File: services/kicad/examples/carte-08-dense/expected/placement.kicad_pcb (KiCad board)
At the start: 2 copper layers, 125 x 95 mm, 56 parts, among them J1 IN_5V, J10 IO0, J11 IO1, J12 IO2, J13 IO3, J14 IO4, J2 SWD, U1 STM32F103C8T6, U2 AMS1117-3.3

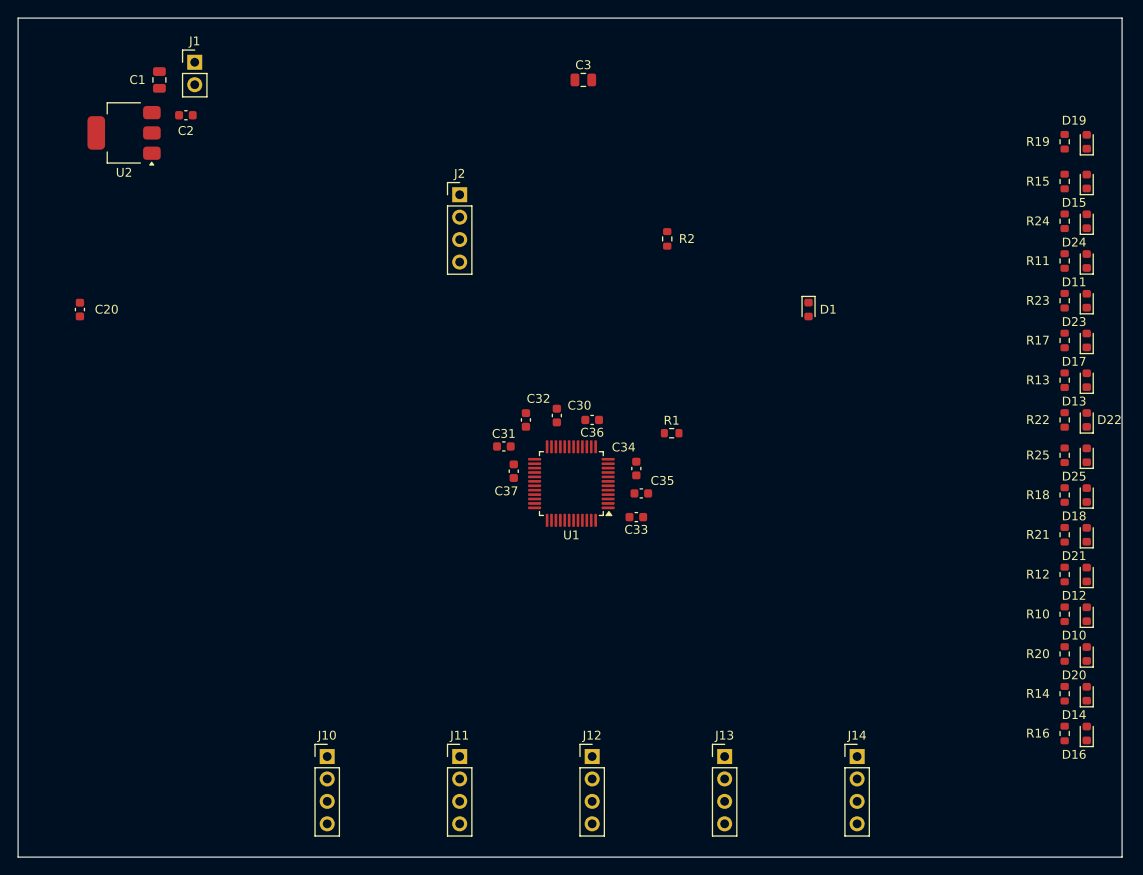
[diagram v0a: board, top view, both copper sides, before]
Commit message: feat(placement): les peripheriques se REPARTISSENT, ils ne s empilent plus
Question de l utilisateur devant le rendu : « c est quoi ce type de placement ? ».
Les composants s entassaient d un seul cote du boitier, etiquettes de
serigraphie l une sur l autre, trois quarts de la couronne vides.

TROIS CAUSES, toutes dans `_poser_les_peripheriques`, toutes la meme faute —
un angle unique pour tout un groupe :

  - les DIRECTS qui visent la meme broche (tous les decouplages d un rail,
    toutes les resistances d un meme signal) recevaient le MEME `angle_vers`
    et le meme rayon de depart ;
  - les SUIVEURS d un meme parent recevaient tous atan2(parent - centre) ;
  - les ISOLES partaient tous de l angle 0.0, c est-a-dire du meme point.

`le_long_du_rayon` ne s ecartait qu une fois la place prise : d ou la file.

REMEDE : `_ecart_en_eventail`. Le PREMIER de chaque groupe garde EXACTEMENT la
direction calculee — c est la topologie, on ne la perd pas pour faire joli — et
les suivants s ecartent symetriquement de 3 x `_PAS_ANGLE_DEG`.
Rien de deja pose ne bouge : seul l ANGLE DE DEPART de la recherche change, et
`le_long_du_rayon` reste seul juge de ce qui est libre.

BANC DES DIX CARTES, contour resserre ET peripheriques repartis :

    carte             demandee    livree         err  manq
    carte-01           25 x 20    20,1 x 13,6     0    0
    carte-02           55 x 40    34,9 x 25,2     0    0
    carte-03           50 x 35    27,6 x 19,9     0    0
    carte-04           60 x 45    36,6 x 29,8     0    0
    carte-05           70 x 50    40,0 x 32,6     0    0
    carte-06           80 x 60    46,5 x 36,4     0    0
    carte-07          110 x 80    47,7 x 38,8     0    0
    carte-08          125 x 95    57,4 x 44,1     0    0
    carte-09          130 x 100   57,8 x 45,2     0    0
    carte-10          140 x 105   59,0 x 45,8     0    0

Dix sur dix, 100 % route. carte-07 gagne 5,5 mm de largeur sur le passage
precedent, carte-06 deux, carte-10 deux. Sur ca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
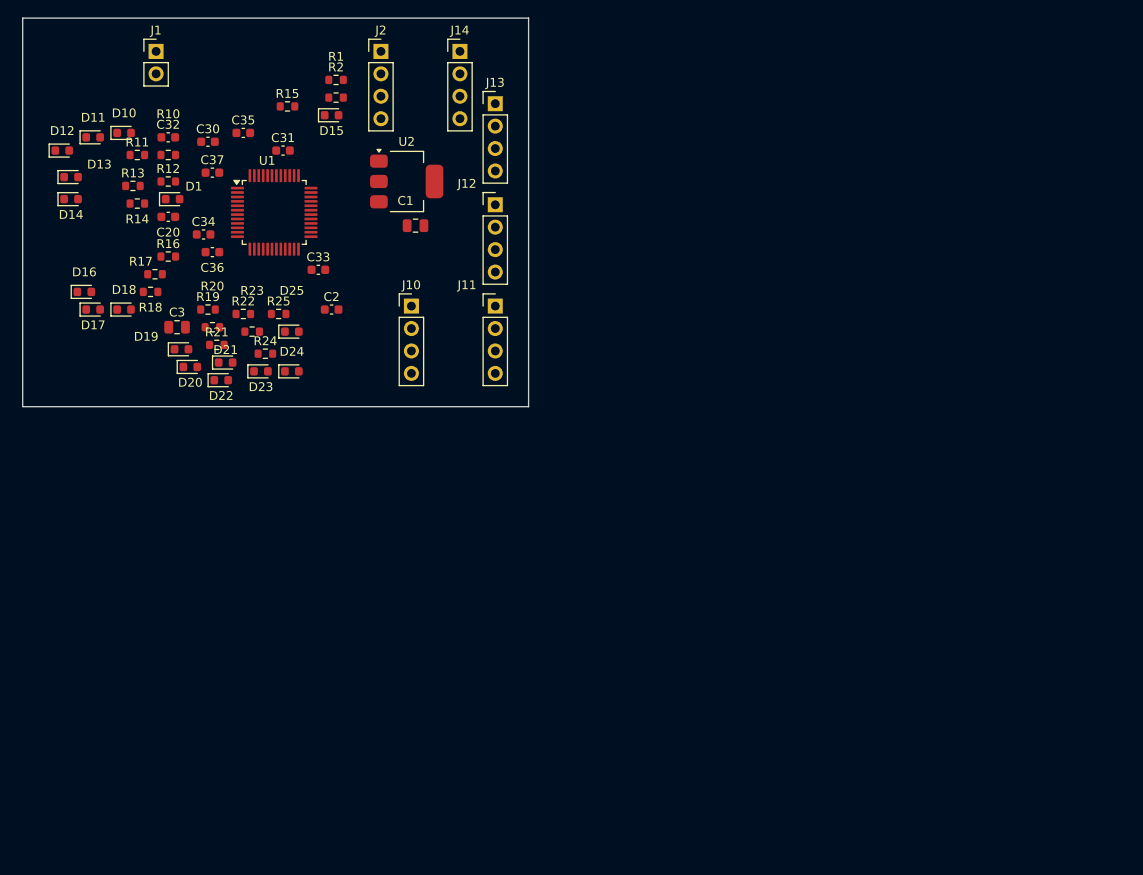
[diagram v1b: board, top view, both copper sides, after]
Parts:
- moved D14 127.9 mm to (92.0, 78.0), turned to 0 degrees
- moved D12 125.5 mm to (91.0, 72.5), turned to 0 degrees
- moved D16 124.0 mm to (93.5, 88.5), turned to 0 degrees
- moved D10 121.9 mm to (98.0, 70.5), turned to 0 degrees
- moved R14 118.8 mm to (99.5, 78.5), turned to 0 degrees
- moved D13 117.3 mm to (92.0, 75.5), turned to 0 degrees
- moved R16 115.0 mm to (103.0, 84.5), turned to 0 degrees
- moved R10 114.0 mm to (103.0, 73.0), turned to 0 degrees
- moved D11 113.4 mm to (94.5, 71.0), turned to 0 degrees
- moved D17 112.6 mm to (94.5, 90.5), turned to 0 degrees
- moved D18 111.0 mm to (98.0, 90.5), turned to 0 degrees
- moved R12 110.8 mm to (103.0, 76.0), turned to 0 degrees
- moved R13 107.8 mm to (99.0, 76.5), turned to 0 degrees
- moved D20 106.6 mm to (105.5, 97.0), turned to 0 degrees
- moved R18 106.0 mm to (101.0, 88.5), turned to 0 degrees
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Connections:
- U1 pad 36: Net-(U1-36) -> PWR_FLAG
- U1 pad 48: Net-(U1-48) -> PWR_FLAG
- U1 pad 9: IO_L5 -> PWR_FLAG
- U2 pad 3: VIN -> PWR_FLAG
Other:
- board size 125 x 95 mm -> 57.3 x 44 mm

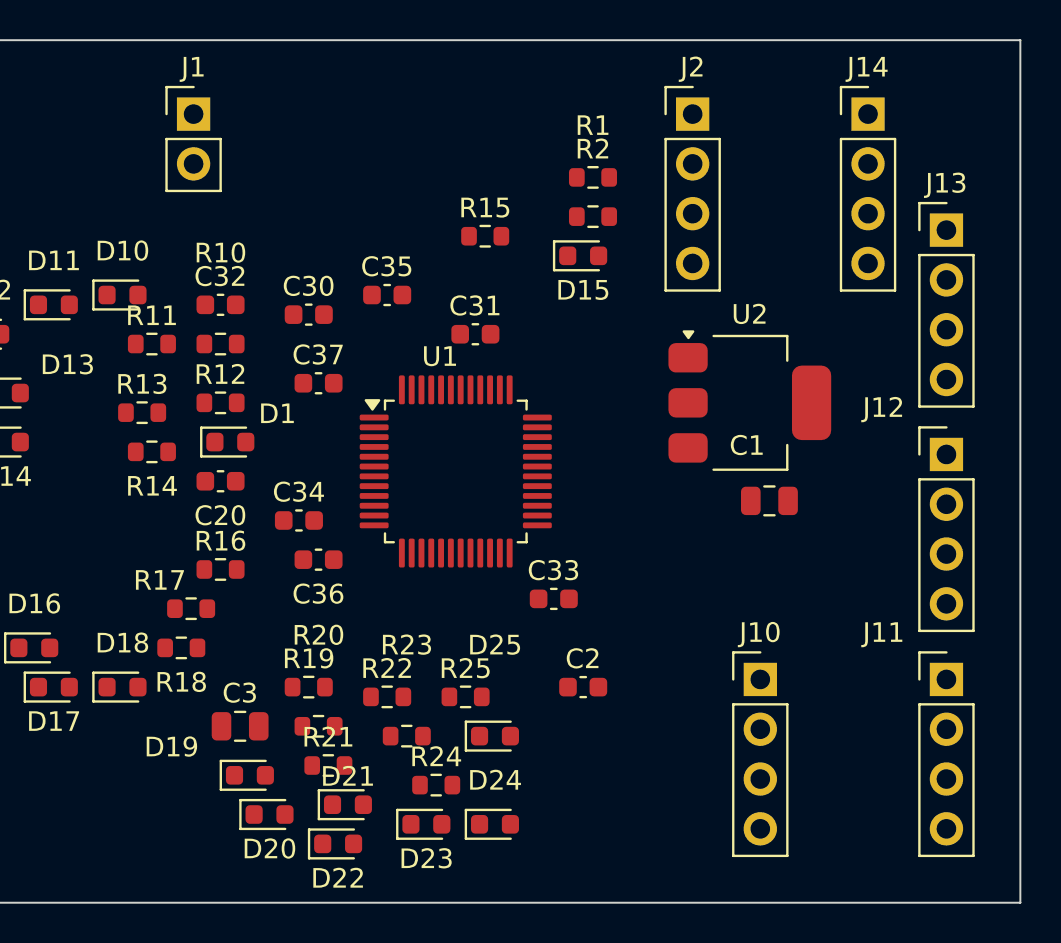
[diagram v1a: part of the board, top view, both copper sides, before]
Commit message: docs(banc): les dix boards du banc du 2026-09-23, service corrige
Artefacts du banc dont le tableau est deja commite : les dix cartes a
100 % route, 0 erreur, 0 connexion manquante, chacune a la taille de son
circuit.

Co-Authored-By: Claude Opus 5 <noreply@anthropic.com>
Claude-Session: https://claude.ai/code/session_01TnMqm4La2CxQHHB5K8aSSV
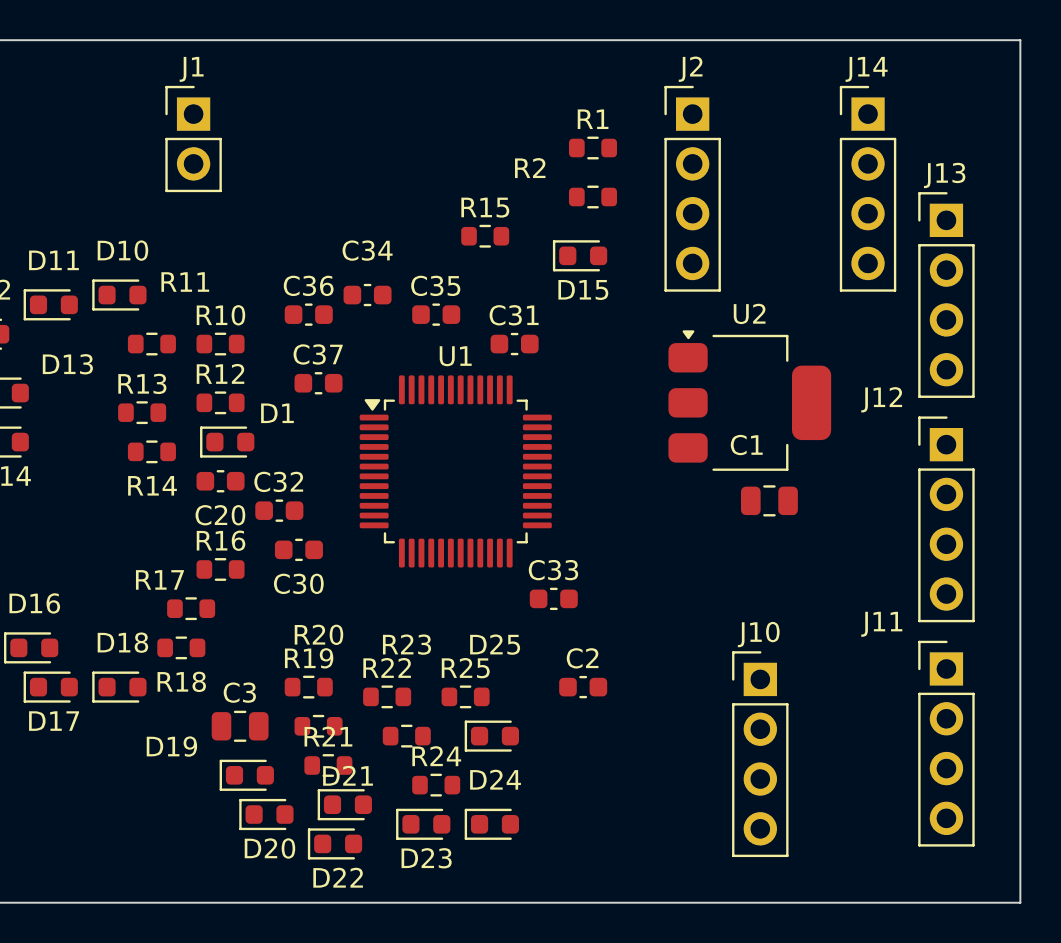
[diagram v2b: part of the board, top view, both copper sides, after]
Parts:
- moved C36 12.5 mm to (107.5, 71.5)
- moved C34 12.0 mm to (110.5, 70.5)
- moved C30 12.0 mm to (107.0, 83.5)
- moved C32 10.9 mm to (106.0, 81.5)
- moved R1 3.50 mm to (122.0, 63.0)
- moved C35 2.69 mm to (114.0, 71.5)
- moved C31 2.06 mm to (118.0, 73.0)
- moved R2 1.00 mm to (122.0, 65.5)
- moved J11 0.53 mm to (140.0, 89.6)
- moved J12 0.50 mm to (140.0, 78.1)
- moved J13 0.50 mm to (140.0, 66.7)
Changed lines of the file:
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@@
 		(tags "LQFP QFP CASE-932AA CASE-932-03 C48-1 C48-2 C48-3 C48-5 C48-6 C48-6C PT0048A")
 		(property "Reference" "U1"
-			(at -0.8 -5.85 0)
+			(at 0 -5.85 0)
 			(layer "F.SilkS")
 			(effects
@@
 		(generator "kicad-footprint-generator")
 		(layer "F.Cu")
-		(at 122 66.5)
+		(at 122 63)
 		(descr "Resistor SMD 0603 (1608 Metric), square (rectangular) end terminal, IPC-7351 nominal, (Body size source: IPC-SM-782 page 72, https://www.pcb-3d.com/wordpress/wp-content/uploads/ipc-sm-782a_amendment_1_and_2.pdf)")
 		(tags "resistor")
 		(property "Reference" "R1"
-			(at -5.8783e-16 -4.63 0)
+			(at 0 -1.43 0)
 			(layer "F.SilkS")
 			(effects
@@
 		(generator "kicad-footprint-generator")
 		(layer "F.Cu")
-		(at 122 64.5)
+		(at 122 65.5)
 		(descr "Resistor SMD 0603 (1608 Metric), square (rectangular) end terminal, IPC-7351 nominal, (Body size source: IPC-SM-782 page 72, https://www.pcb-3d.com/wordpress/wp-content/uploads/ipc-sm-782a_amendment_1_and_2.pdf)")
 		(tags "resistor")
 		(property "Reference" "R2"
-			(at 0 -1.43 0)
+			(at -3.2 -1.43 0)
 			(layer "F.SilkS")
 			(effects
@@
 		(generator "kicad-footprint-generator")
 		(layer "F.Cu")
-		(at 107.5 71.5)
+		(at 107 83.5)
 		(descr "Capacitor SMD 0603 (1608 Metric), square (rectangular) end terminal, IPC-7351 nominal, (Body size source: IPC-SM-782 page 76, https://www.pcb-3d.com/wordpress/wp-content/uploads/ipc-sm-782a_amendment_1_and_2.pdf)")
 		(tags "capacitor")
 		(property "Reference" "C30"
-			(at 0 -1.43 0)
+			(at 1.95943e-16 1.77 0)
 			(layer "F.SilkS")
 			(effects
@@
 		(generator "kicad-footprint-generator")
 		(layer "F.Cu")
-		(at 116 72.5)
+		(at 118 73)
 		(descr "Capacitor SMD 0603 (1608 Metric), square (rectangular) end terminal, IPC-7351 nominal, (Body size source: IPC-SM-782 page 76, https://www.pcb-3d.com/wordpress/wp-content/uploads/ipc-sm-782a_amendment_1_and_2.pdf)")
 		(tags "capacitor")
@@
 		(generator "kicad-footprint-generator")
 		(layer "F.Cu")
-		(at 103 71)
+		(at 106 81.5)
 		(descr "Capacitor SMD 0603 (1608 Metric), square (rectangular) end terminal, IPC-7351 nominal, (Body size source: IPC-SM-782 page 76, https://www.pcb-3d.com/wordpress/wp-content/uploads/ipc-sm-782a_amendment_1_and_2.pdf)")
 		(tags "capacitor")
@@
 		(generator "kicad-footprint-generator")
 		(layer "F.Cu")
-		(at 107 82)
+		(at 110.5 70.5)
 		(descr "Capacitor SMD 0603 (1608 Metric), square (rectangular) end terminal, IPC-7351 nominal, (Body size source: IPC-SM-782 page 76, https://www.pcb-3d.com/wordpress/wp-content/uploads/ipc-sm-782a_amendment_1_and_2.pdf)")
 		(tags "capacitor")
 		(property "Reference" "C34"
-			(at 0 -1.43 0)
+			(at -1.46958e-16 -2.23 0)
 			(layer "F.SilkS")
 			(effects
@@
 		(generator "kicad-footprint-generator")
 		(layer "F.Cu")
-		(at 111.5 70.5)
+		(at 114 71.5)
 		(descr "Capacitor SMD 0603 (1608 Metric), square (rectangular) end terminal, IPC-7351 nominal, (Body size source: IPC-SM-782 page 76, https://www.pcb-3d.com/wordpress/wp-content/uploads/ipc-sm-782a_amendment_1_and_2.pdf)")
 		(tags "capacitor")
@@
 		(generator "kicad-footprint-generator")
 		(layer "F.Cu")
-		(at 108 84)
+		(at 107.5 71.5)
 		(descr "Capacitor SMD 0603 (1608 Metric), square (rectangular) end terminal, IPC-7351 nominal, (Body size source: IPC-SM-782 page 76, https://www.pcb-3d.com/wordpress/wp-content/uploads/ipc-sm-782a_amendment_1_and_2.pdf)")
 		(tags "capacitor")
 		(property "Reference" "C36"
-			(at 1.95943e-16 1.77 0)
+			(at 0 -1.43 0)
 			(layer "F.SilkS")
 			(effects
@@
 		(tags "resistor")
 		(property "Reference" "R10"
-			(at -5.8783e-16 -4.63 0)
+			(at 0 -1.43 0)
 			(layer "F.SilkS")
 			(effects
@@
 		(tags "resistor")
 		(property "Reference" "R11"
-			(at 0 -1.43 0)
+			(at 1.69706 -3.12706 0)
 			(layer "F.SilkS")
 			(effects
@@
 		(generator "kicad-footprint-generator")
 		(layer "F.Cu")
-		(at 140.03 90.11)
+		(at 140.03 89.5759)
 		(descr "Through hole straight pin header, 1x04, 2.54mm pitch, single row")
 		(tags "Through hole pin header THT 1x04 2.54mm single row")
@@
 		(generator "kicad-footprint-generator")
 		(layer "F.Cu")
-		(at 140.03 78.6329)
+		(at 140.03 78.1329)
 		(descr "Through hole straight pin header, 1x04, 2.54mm pitch, single row")
 		(tags "Through hole pin header THT 1x04 2.54mm single row")
@@
 		(generator "kicad-footprint-generator")
 		(layer "F.Cu")
-		(at 140.03 67.19)
+		(at 140.03 66.69)
 		(descr "Through hole straight pin header, 1x04, 2.54mm pitch, single row")
 		(tags "Through hole pin header THT 1x04 2.54mm single row")
